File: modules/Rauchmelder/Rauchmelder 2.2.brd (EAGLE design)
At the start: 38 x 65 mm, 48 parts, among them IC1 MC34063AD, IC3 LPC922FDH, Q1 BC856, Q3 BCP52, T1 BC848

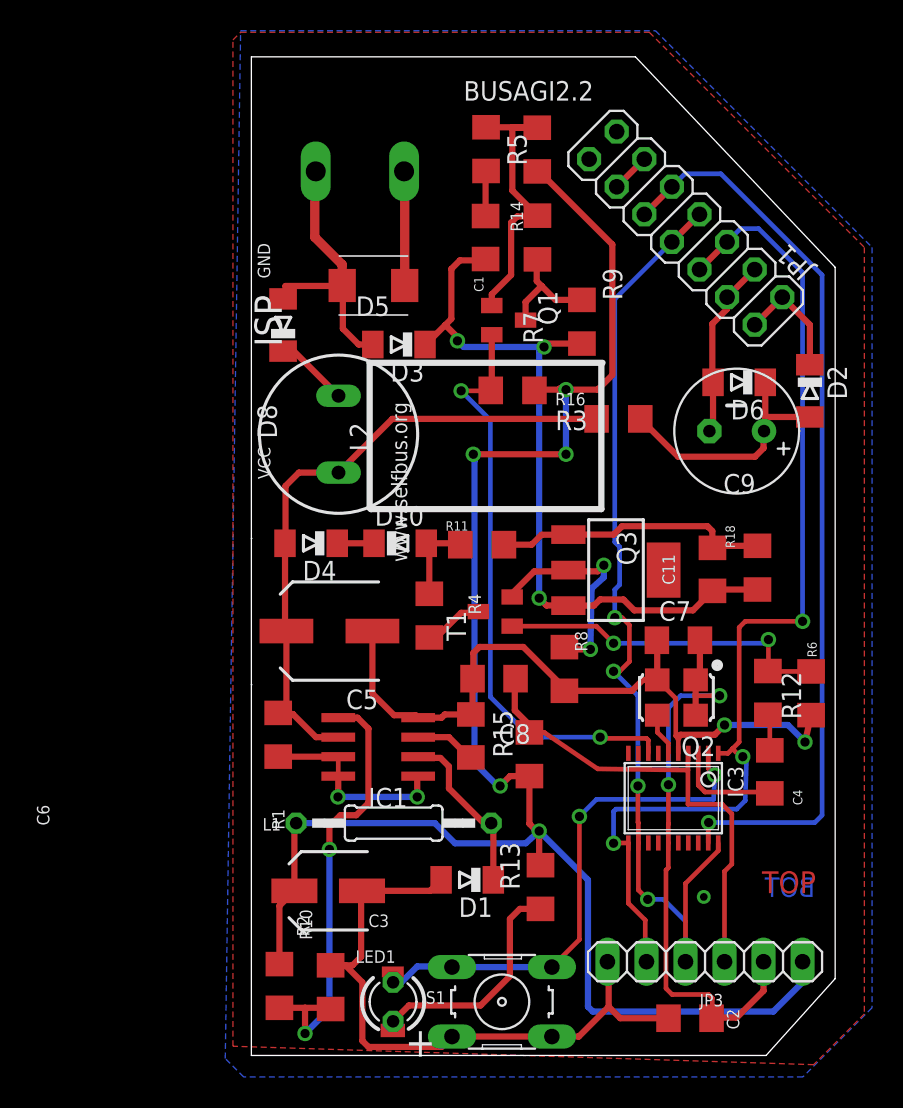
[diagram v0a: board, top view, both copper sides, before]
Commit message: Kosmetik am Rauchmelder 2.2
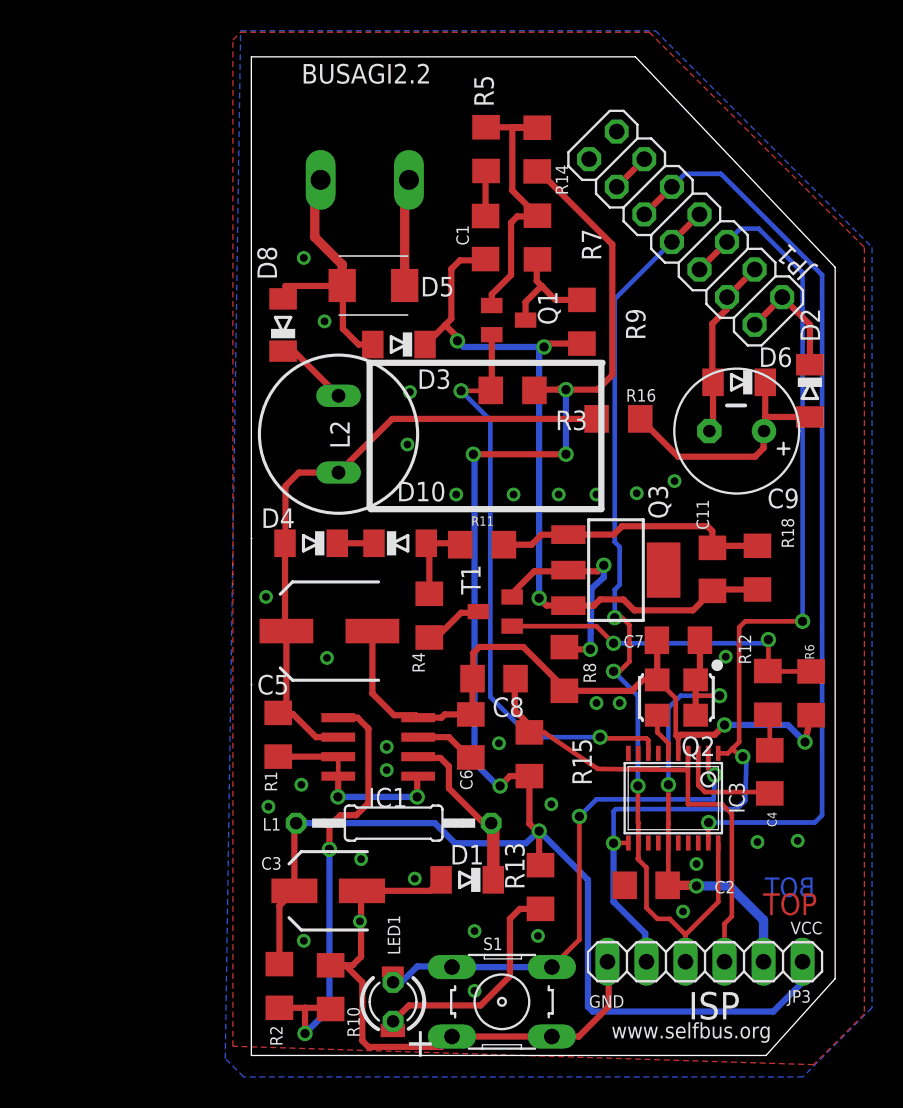
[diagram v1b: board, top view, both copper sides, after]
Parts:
- moved C2 9.11 mm to (25.7, 11.1)
- moved U$1 0.64 mm to (7.38, 57.0)
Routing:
- net N$6: track 39.2 -> 31.7 mm, vias 2 -> 3
- net GND: track 116.4 -> 112.7 mm, vias 3 -> 34
- net TX: track 63.7 -> 61.8 mm, vias 4 -> 3
- net EIB+: track 18.1 -> 18.7 mm
- net RX: track 69.1 -> 69.5 mm, vias 3 -> 4
